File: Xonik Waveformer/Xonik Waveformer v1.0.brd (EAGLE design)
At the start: 160 x 100 mm, 84 parts, among them IC1 TL074D, IC2 TL074D, IC3 TL074D, IC4 4013D, IC5 TL072D

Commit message: Working with board layout
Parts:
- removed R21, R31, R32, R33, R34, R42, R43, R57: 1k, resistor:R0805
- removed R51, R52, R54: 100k, resistor:RTRIM3296W
- removed R53: 50k, resistor:RTRIM3296W
- added +15V, +5V, -15V, CENTER, DCO_IN, DCO_TIMER, GND, INV_SAW, PULSE, PULSE_AMP_CV, PW_CV, SAW, SINE, ST1, ST2, ST3, ST4, SUB_SAW_1, SUB_SAW_2, SUB_SQR2, SUB_SQR_1, SYMMETRY, TRIANGLE: (no value), joakim:MA01-1J
- C5, C6: value (none) -> 100nF
- D1, D2, D3, D4: value (none) -> 1N41480805; device diode:D-5 -> joakim:D0805-J
- IC4: value 4013D -> TL072D; device joakim:SO14J -> joakim:SO08J
- IC5: value TL072D -> 4013D; device joakim:SO08J -> joakim:SO14J
- R9: value 1k -> 330k
- T1: value (none) -> 2n3904
- moved C16 190.9 mm to (58.4, 71.1), turned to 90 degrees
- moved C15 182.0 mm to (52.1, 71.1), turned to 90 degrees
- moved C14 173.0 mm to (45.7, 71.1), turned to 90 degrees
- moved C13 164.1 mm to (39.4, 71.1), turned to 90 degrees
- moved C12 155.1 mm to (33.0, 71.1), turned to 90 degrees
- moved C11 146.2 mm to (26.7, 71.1), turned to 90 degrees
- moved C10 137.3 mm to (20.3, 71.1), turned to 90 degrees
- moved C9 128.3 mm to (14.0, 71.1), turned to 90 degrees
- moved C8 119.4 mm to (7.62, 71.1), turned to 90 degrees
- moved C1 110.5 mm to (45.7, 9.53), turned to 180 degrees
- moved D4 104.9 mm to (24.8, 35.6)
- moved D3 103.6 mm to (24.8, 38.1), turned to 180 degrees
- moved IC4 101.9 mm to (47.0, 21.6)
- moved R30 101.2 mm to (46.4, 12.1), turned to 180 degrees
- moved IC5 98.7 mm to (55.2, 21.6)
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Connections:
- removed net N$25: IC3.14, R38.2, R52.2, R52.3
- removed net N$42: C13.2, C9.1
- removed net N$43: C10.1, C14.2
- removed net N$44: C11.1, C15.2
- removed net V+: IC5.8
- removed net V-: IC5.4
- new net N$41: IC3.8, R38.2, ST2.1
- net +15V: now also +15V.1, C10.2, C11.2, C9.2, IC4.8
- net +5V: now also +5V.1, IC5.14; no longer IC4.14
- net -15V: now also -15V.1, C13.1, C14.1, C15.1, IC4.4; no longer R54.2, R54.3
- net AMP_CV: now also PULSE_AMP_CV.1
- net DCO_IN: now also DCO_IN.1
- net GND: now also C10.1, C11.1, C13.2, C14.2, C15.2, C9.1, GND.1, IC1.10, IC4.3, IC4.5, IC5.10, IC5.4, IC5.6, IC5.7, IC5.8; no longer IC1.5, IC2.10, IC4.10, IC4.4, IC4.6, IC4.7, IC4.8, IC5.3
- net N$10: now also CENTER.1, IC1.2; no longer IC1.6, R54.1
- net N$11: now also IC1.9; no longer IC1.2
- net N$12: now also IC1.8; no longer IC1.1
- net N$14: now also IC2.13; no longer IC5.2
- net N$15: now also IC2.2; no longer IC2.13
- net N$16: now also IC2.1, SAW.1; no longer IC2.14, R32.1
- net N$17: now also IC4.7, SUB_SQR_1.1; no longer IC2.8, R33.1
- net N$18: now also IC4.1, SUB_SQR2.1; no longer IC2.1, R34.1
- net N$19: now also IC4.6; no longer IC2.9
- net N$20: now also ST4.1; no longer R51.2, R51.3
- net N$22: now also IC4.2; no longer IC2.2
- net N$24: now also IC3.9, ST1.1; no longer IC3.13, R52.1
- net N$26: now also IC3.13; no longer IC3.9
- net N$27: now also IC3.14, SUB_SAW_1.1; no longer IC3.8, R42.1
- net N$28: now also ST3.1; no longer R51.1
- net N$3: now also R9.1
- net N$30: now also SUB_SAW_2.1; no longer R43.1
- net N$31: now also IC5.2, IC5.5; no longer IC4.2, IC4.5
- net N$32: now also IC5.1, IC5.11; no longer IC4.1, IC4.11
- net N$34: now also IC5.12, IC5.9; no longer IC4.12, IC4.9
- net N$35: now also IC5.13; no longer IC4.13
- net N$36: now also IC2.9; no longer IC5.6
- net N$37: now also SYMMETRY.1; no longer R53.2
- net N$38: now also IC2.14, TRIANGLE.1; no longer IC5.1, R57.1
- net N$39: now also IC2.10; no longer IC5.5
- net N$40: now also IC2.8, SINE.1; no longer IC5.7, R21.2
- net N$6: now also IC1.6; no longer IC1.9
- net N$7: now also IC1.7, PULSE.1; no longer IC1.8, R9.1
- net N$8: now also IC1.5; no longer IC1.10
- net N$9: now also IC1.1, INV_SAW.1; no longer IC1.7, R31.1
- net PW_CV: now also PW_CV.1
- net SQR: now also DCO_TIMER.1, IC5.3; no longer IC4.3
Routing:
- net -15V: track 0.00 -> 48.7 mm
- net +15V: track 0.00 -> 48.7 mm
- net -2.5V: track 0.00 -> 41.3 mm, vias 0 -> 6
- net GND: track 0.00 -> 39.7 mm
- net N$9: track 0.00 -> 11.2 mm
- net N$10: track 0.00 -> 8.16 mm
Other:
- board size 160 x 100 mm -> 61 x 100 mm

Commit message: Still doing layout
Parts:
- removed TP1: TPPAD1-13, testpad:P1-13
- moved R4 15.3 mm to (13.3, 20.3)
- moved C3 11.0 mm to (29.8, 24.8), turned to 270 degrees
- moved R26 9.55 mm to (55.2, 29.8), turned to 90 degrees
- moved D3 8.64 mm to (22.2, 29.8), turned to 90 degrees
- moved R41 8.28 mm to (32.4, 24.8), turned to 270 degrees
- moved R1 8.28 mm to (6.35, 27.9), turned to 90 degrees
- moved R20 7.85 mm to (32.4, 29.8), turned to 90 degrees
- moved R29 7.67 mm to (52.7, 29.8), turned to 90 degrees
- moved R36 7.67 mm to (45.1, 29.8), turned to 90 degrees
- moved C2 7.24 mm to (50.2, 29.8), turned to 90 degrees
- moved R2 7.24 mm to (5.08, 32.4), turned to 90 degrees
- moved R35 6.54 mm to (34.9, 29.8), turned to 90 degrees
- moved C4 6.02 mm to (29.8, 18.4), turned to 90 degrees
- moved R40 5.75 mm to (37.5, 29.8), turned to 270 degrees
- moved D4 5.72 mm to (24.8, 29.8), turned to 270 degrees
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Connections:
- net N$9: no longer TP1.TP
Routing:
- net GND: track 39.7 -> 198.6 mm, vias 0 -> 10
- net N$17: track 0.00 -> 48.8 mm, vias 0 -> 1
- net N$16: track 0.00 -> 47.1 mm, vias 0 -> 3
- net N$18: track 0.00 -> 35.4 mm
- net N$40: track 0.00 -> 35.4 mm, vias 0 -> 2
- net N$27: track 0.00 -> 34.7 mm, vias 0 -> 2
- net -15V: track 48.7 -> 82.7 mm, vias 0 -> 4
- net N$41: track 0.00 -> 31.2 mm, vias 0 -> 1
- net N$24: track 0.00 -> 27.6 mm, vias 0 -> 2
- net -2.5V: track 41.3 -> 67.5 mm, vias 6 -> 7
- net +5V: track 0.00 -> 24.6 mm, vias 0 -> 1
- net +15V: track 48.7 -> 72.8 mm, vias 0 -> 3
- net N$26: track 0.00 -> 23.0 mm
- net N$30: track 0.00 -> 22.7 mm, vias 0 -> 1
- net N$28: track 0.00 -> 18.7 mm, vias 0 -> 1
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
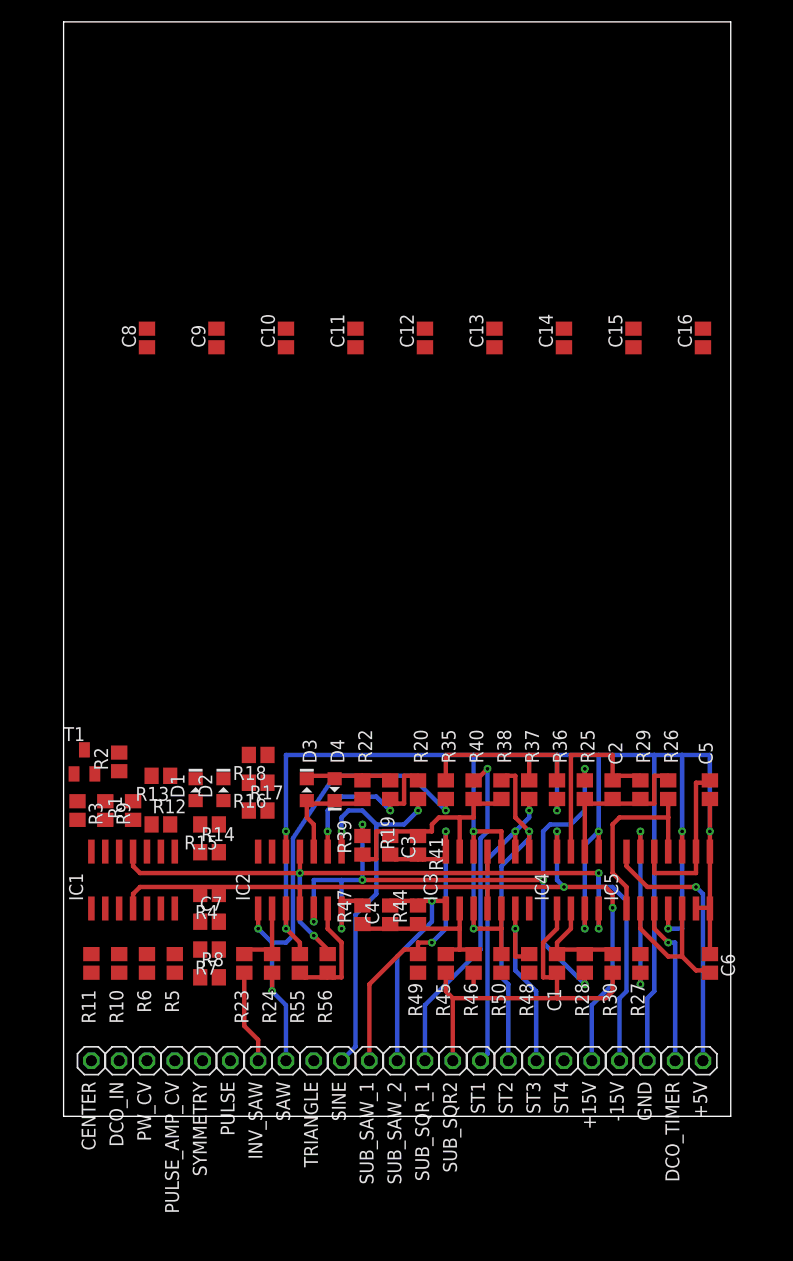
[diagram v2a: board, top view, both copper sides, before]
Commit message: Routing complete except for bypass caps
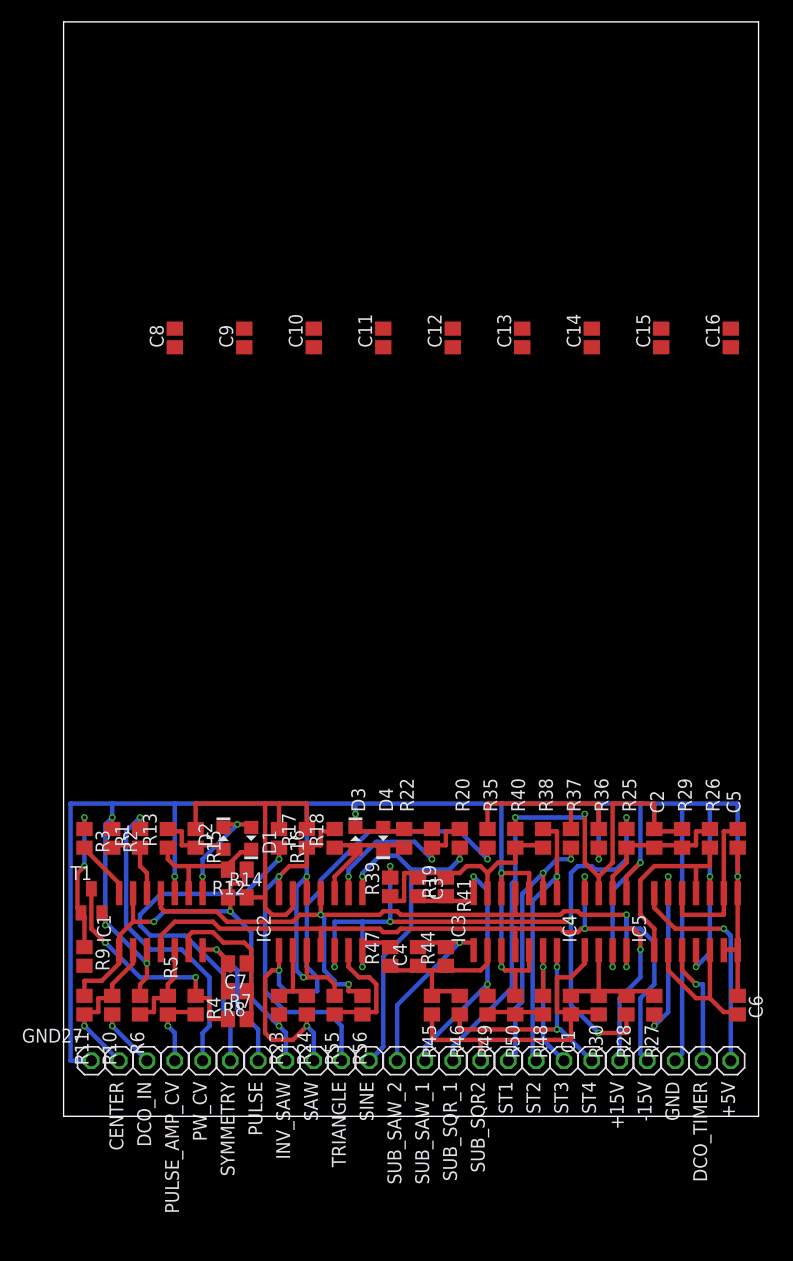
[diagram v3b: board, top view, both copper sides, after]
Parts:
- added GND27: (no value), joakim:MA01-1J
- moved R9 13.5 mm to (1.91, 14.6)
- moved T1 12.7 mm to (2.54, 19.7)
- moved R18 10.3 mm to (24.8, 25.4), turned to 90 degrees
- moved R4 10.2 mm to (12.1, 10.2), turned to 270 degrees
- moved R12 8.11 mm to (15.9, 22.5), turned to 180 degrees
- moved R49 7.41 mm to (38.7, 10.2)
- moved R2 7.01 mm to (4.45, 25.4), turned to 270 degrees
- moved R7 6.84 mm to (15.9, 8.89), turned to 0 degrees
- moved D1 6.75 mm to (17.1, 25.4), turned to 270 degrees
- moved D3 6.29 mm to (26.7, 25.4)
- moved D4 6.29 mm to (29.2, 25.4)
- moved C2 5.85 mm to (54.0, 25.4)
- moved R19 5.85 mm to (33.7, 25.4)
- moved R20 5.85 mm to (36.2, 25.4)
- moved R25 5.85 mm to (51.4, 25.4)
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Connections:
- removed net N$8: IC1.5, R6.2
- net GND: now also GND27.1, R6.2
- net N$5: now also IC1.5
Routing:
- net GND: track 198.6 -> 274.8 mm, vias 10 -> 15
- net N$9: track 8.57 -> 43.8 mm, vias 0 -> 3
- net N$37: track 0.00 -> 34.5 mm, vias 0 -> 1
- net N$14: track 0.00 -> 32.7 mm
- net N$38: track 0.00 -> 32.7 mm, vias 0 -> 1
- net PW_CV: track 0.00 -> 28.9 mm, vias 0 -> 1
- net N$4: track 0.00 -> 21.8 mm, vias 0 -> 2
- net N$20: track 1.05 -> 21.9 mm, vias 0 -> 2
- net N$7: track 0.00 -> 19.7 mm, vias 0 -> 1
- net N$6: track 0.00 -> 15.5 mm
- net N$10: track 0.00 -> 14.7 mm, vias 0 -> 1
- net N$3: track 0.00 -> 13.4 mm, vias 0 -> 2
- net N$11: track 0.00 -> 12.6 mm
- net N$12: track 0.00 -> 10.5 mm, vias 0 -> 2
- net N$5: track 0.00 -> 8.67 mm
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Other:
- board size 61 x 100 mm -> 63.5 x 100 mm

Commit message: Finished tracing, working on labels
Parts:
- C10, C11, C12, C13, C14, C15, C8, C9: device resistor:C0805 -> resistor:C0603K
- moved C15 66.3 mm to (14.0, 18.7), flipped to the bottom, turned to 0 degrees
- moved C8 65.9 mm to (48.9, 17.8), flipped to the bottom, turned to 270 degrees
- moved C16 61.0 mm to (61.6, 10.2), turned to 270 degrees
- moved C9 60.9 mm to (44.1, 16.8), flipped to the bottom, turned to 180 degrees
- moved C14 56.5 mm to (27.0, 18.7), flipped to the bottom, turned to 0 degrees
- moved C11 56.4 mm to (14.0, 16.8), flipped to the bottom, turned to 180 degrees
- moved C12 56.0 mm to (52.7, 17.8), flipped to the bottom
- moved C10 54.4 mm to (27.0, 16.8), flipped to the bottom, turned to 180 degrees
- moved C13 52.4 mm to (44.1, 18.7), flipped to the bottom, turned to 0 degrees
- moved C6 2.54 mm to (59.1, 10.2)
- turned GND27 to 90 degrees
- renumbered R1 to 1, R10 to 10, R11 to 11, R12 to 12, R13 to 13, R14 to 14, R15 to 15, R16 to 16, R17 to 17, R18 to 18, R19 to 19, R2 to 2, R20 to 20, R22 to 22, R23 to 23, R24 to 24, R25 to 25, R26 to 26, R27 to 27, R28 to 28, R29 to 29, R3 to 3, R30 to 30, R35 to 35, R36 to 36, R37 to 37, R38 to 38, R39 to 39, R4 to 4, R40 to 40, R41 to 41, R44 to 44, R45 to 45, R46 to 46, R47 to 47, R48 to 48, R49 to 49, R5 to 5, R50 to 50, R55 to 55, R56 to 56, R6 to 6, R7 to 7, R8 to 8, R9 to 9
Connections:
- net GND: now also 9.2
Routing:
- net GND: track 274.8 -> 307.9 mm, vias 15 -> 19
- net +15V: track 69.2 -> 75.0 mm, vias 3 -> 6
- net -15V: track 81.8 -> 86.1 mm, vias 4 -> 7
- net -2.5V: track 73.3 -> 70.1 mm
- net N$9: track 43.8 -> 46.5 mm
- net N$24: track 24.4 -> 26.6 mm
- net N$41: track 24.8 -> 26.7 mm
- net N$30: track 20.0 -> 21.4 mm
- net +5V: track 20.8 -> 22.2 mm, vias 1 -> 2
- net N$17: track 56.6 -> 57.9 mm
- net N$31: track 14.4 -> 13.2 mm
- net N$16: track 52.8 -> 53.4 mm
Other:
- board size 63.5 x 100 mm -> 63.5 x 29.8 mm

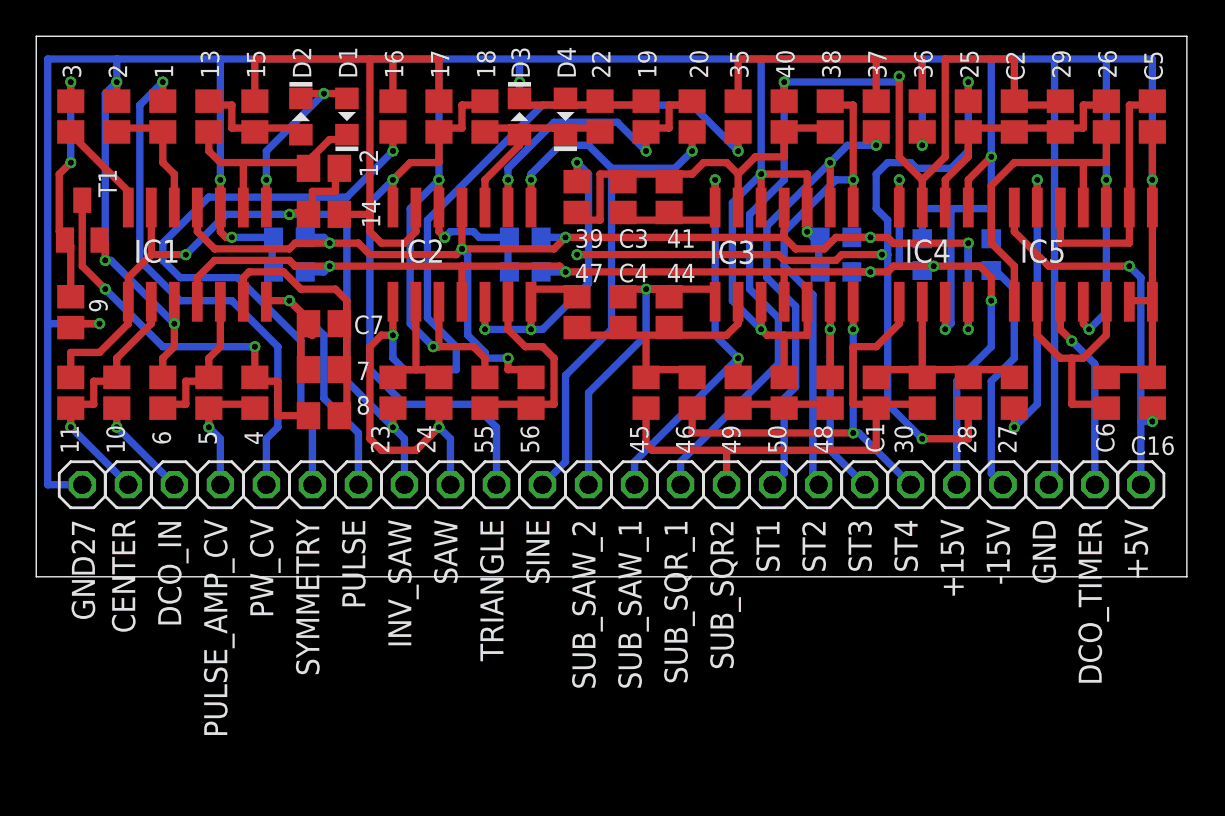
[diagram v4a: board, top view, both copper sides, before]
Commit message: Trace and text complete, gp and logo missing
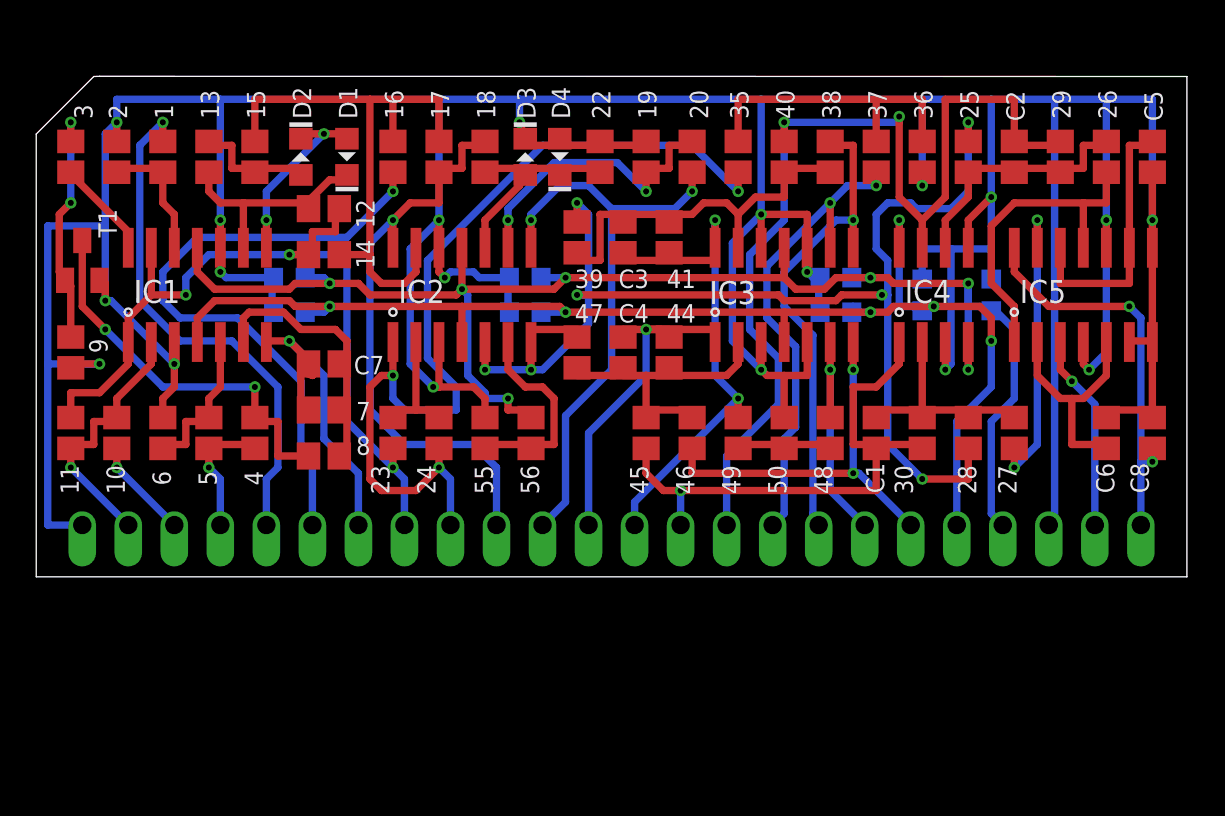
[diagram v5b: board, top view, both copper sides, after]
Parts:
- removed SUB_SQR2: (no value), joakim:MA01-1J
- added SUB_SQR_2: (no value), joakim:SIP-PIN01-1J
- +15V, +5V, -15V, CENTER, DCO_IN, DCO_TIMER, GND, GND27, INV_SAW, PULSE, PULSE_AMP_CV, PW_CV, SAW, SINE, ST1, ST2, ST3, ST4, SUB_SAW_1, SUB_SAW_2, SUB_SQR_1, SYMMETRY, TRIANGLE: device joakim:MA01-1J -> joakim:SIP-PIN01-1J
- C16: device resistor:C0805 -> resistor:C0603K
- C8: device resistor:C0603K -> resistor:C0805
- moved C8 16.1 mm to (61.6, 7.94), flipped to the top
- moved C16 13.8 mm to (48.9, 15.6), flipped to the bottom
- moved SUB_SQR_1 3.38 mm to (38.1, 2.86), turned to 0 degrees
- moved D4 2.25 mm to (28.9, 23.2)
- moved D3 2.25 mm to (27.0, 23.2)
- moved C12 2.22 mm to (52.7, 15.6)
- moved IC1 2.22 mm to (8.89, 15.6)
- moved IC2 2.22 mm to (23.5, 15.6)
- moved IC3 2.22 mm to (41.3, 15.6)
- moved IC4 2.22 mm to (49.5, 15.6)
- moved IC5 2.22 mm to (57.8, 15.6)
- moved +15V 2.22 mm to (50.8, 2.86), turned to 0 degrees
- moved +5V 2.22 mm to (61.0, 2.86), turned to 0 degrees
- moved -15V 2.22 mm to (53.3, 2.86), turned to 0 degrees
- moved 1 2.22 mm to (6.99, 23.2)
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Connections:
- net +15V: now also C16.2; no longer C8.2
- net +5V: now also C8.2; no longer C16.2
- net N$18: now also SUB_SQR_2.1; no longer SUB_SQR2.1
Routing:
- net GND: track 307.9 -> 300.3 mm
- net N$17: track 57.9 -> 56.8 mm
- net N$9: track 46.5 -> 47.3 mm
- net N$18: track 30.7 -> 30.3 mm, vias 0 -> 1
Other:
- board size 63.5 x 29.8 mm -> 63.5 x 27.6 mm
- board text added: "+15V"
- board text added: "+5V"
- board text added: "-15V"
- board text added: "Center"
- board text added: "DCO in"
- board text added: "GND"
- board text added: "PW CV"
- board text added: "Pulse"
- board text added: "Pulse VCA"
- board text added: "Saw"
- board text added: "Saw 1"
- board text added: "Saw 1 match"
- board text added: "Saw 2"
- board text added: "Saw 2 match"
- board text added: "Saw inv"
- board text added: "Sine"
- board text added: "Sqr 1"
- board text added: "Sqr 2"
- board text added: "Sub oscillator"
- board text added: "Symmetry"
- board text added: "Timer in"
- board text added: "Triangle"
